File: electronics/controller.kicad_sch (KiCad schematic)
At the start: 81 parts, among them J1 Conn_01x02, J10 Heated_Bed_Thermistor_Connect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, J11 Bl_Touch_Gnd_ZMin_Connector, J12 Bl_Touch_Signal_Vcc_Gnd_Conne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, J13 Motor_A_Connector, J14 Motor_B_Connector, J15 Motor_Z_Connector, J16 Motor_E_Connector, J2 X_Axis_Endstop_Connector, J3 Y_Axis_Endstop_Connector, J4 USB_C_Receptacle_USB2.0, J5 Hotend_Connector, J6 Heated_Bed_Connector, J7 Hotend_Fan_Connector, J8 Layer_Fan_Connector, J9 Hotend_Thermistor_Connector, Q1 PSMN4R1-30YLC, Q2 PSMN4R1-30YLC, Q3 PSMN4R1-30YLC, Q4 PSMN4R1-30YLC, SW1 EN_Button, SW2 Boot_Button, SW3 Pause/Resume_Button, U1 K7803JT-500R3-LB, U2 LMTOE78_05-0.5, U3 ESP32-S3-WROOM-1, U4 MT29F2G01ABAGDWB-IT, U5 USBLC6-2SC6, U6 TMC2209_SILENTSTEPSTICK, U7 TMC2209_SILENTSTEPSTICK, U8 TMC2209_SILENTSTEPSTICK, U9 TMC2209_SILENTSTEPSTICK

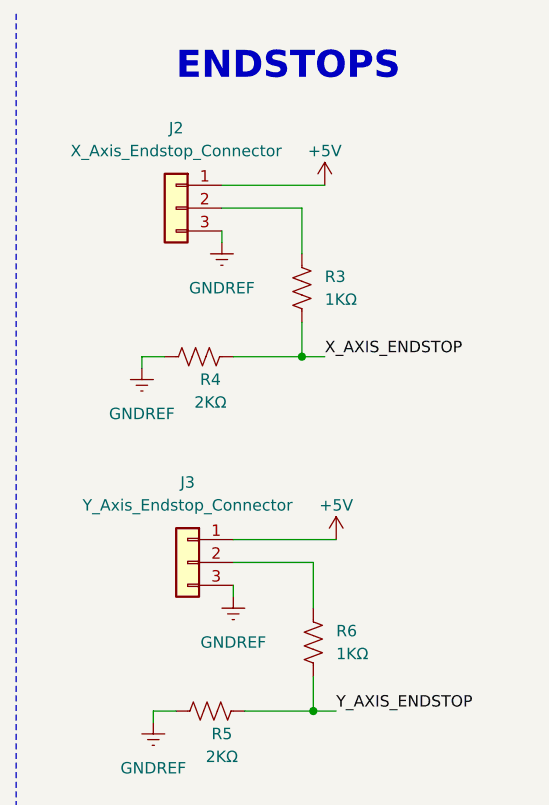
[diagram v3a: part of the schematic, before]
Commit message: ✨ Add filter capacitors to endstops on KiCad schematic
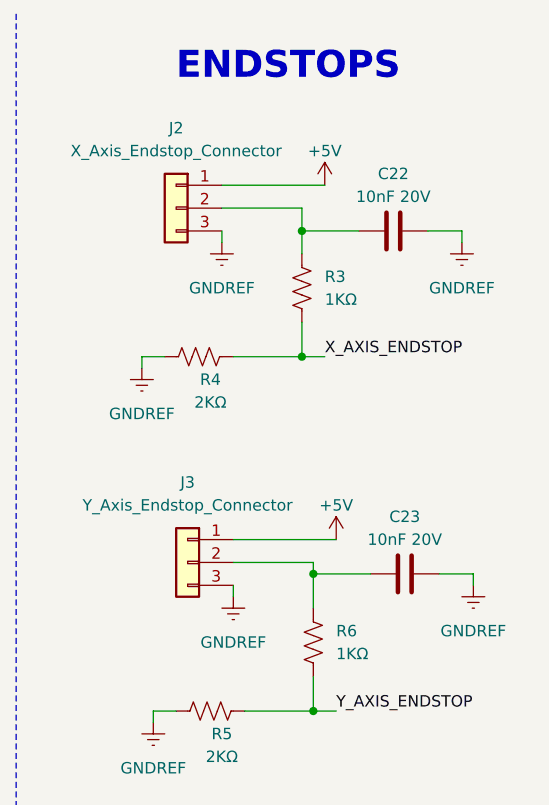
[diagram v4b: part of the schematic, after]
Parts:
- added C22, C23: 10nF 20V, symbol Project:C
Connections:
- net GNDREF: now also C22.2, C23.2
- net at J3.2 (Pin_2), R6.2: now also C23.1
- net at J2.2 (Pin_2), R3.2: now also C22.1
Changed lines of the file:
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@@
   (junction (at 229.87 43.18) (diameter 0) (color 0 0 0 0)
   )
+  (junction (at 383.54 35.56) (diameter 0) (color 0 0 0 0)
+  )
   (junction (at 280.67 229.87) (diameter 0) (color 0 0 0 0)
   )
@@
   (junction (at 121.92 208.28) (diameter 0) (color 0 0 0 0)
   )
+  (junction (at 384.81 73.66) (diameter 0) (color 0 0 0 0)
+  )
   (no_connect (at 256.54 114.3))
   (no_connect (at 43.18 259.08))
@@
     (stroke (width 0) (type default))
   )
-  (wire (pts (xy 384.81 72.39) (xy 384.81 77.47))
+  (wire (pts (xy 384.81 72.39) (xy 384.81 73.66))
     (stroke (width 0) (type default))
   )
@@
     (stroke (width 0) (type default))
   )
+  (wire (pts (xy 389.89 35.56) (xy 383.54 35.56))
+    (stroke (width 0) (type default))
+  )
   (wire (pts (xy 227.33 247.65) (xy 227.33 243.84))
     (stroke (width 0) (type default))
@@
     (stroke (width 0) (type default))
   )
+  (wire (pts (xy 402.59 74.93) (xy 402.59 73.66))
+    (stroke (width 0) (type default))
+  )
   (wire (pts (xy 242.57 247.65) (xy 246.38 247.65))
     (stroke (width 0) (type default))
@@
     (stroke (width 0) (type default))
   )
+  (wire (pts (xy 401.32 36.83) (xy 401.32 35.56))
+    (stroke (width 0) (type default))
+  )
   (wire (pts (xy 80.01 180.34) (xy 86.36 180.34))
     (stroke (width 0) (type default))
@@
     (stroke (width 0) (type dash))
   )
+  (wire (pts (xy 397.51 35.56) (xy 401.32 35.56))
+    (stroke (width 0) (type default))
+  )
   (wire (pts (xy 27.94 248.92) (xy 43.18 248.92))
     (stroke (width 0) (type default))
@@
     (stroke (width 0) (type default))
   )
-  (wire (pts (xy 383.54 33.02) (xy 383.54 38.1))
+  (wire (pts (xy 383.54 33.02) (xy 383.54 35.56))
     (stroke (width 0) (type default))
   )
@@
     (stroke (width 0) (type default))
   )
+  (wire (pts (xy 398.78 73.66) (xy 402.59 73.66))
+    (stroke (width 0) (type default))
+  )
   (wire (pts (xy 44.45 114.3) (xy 64.77 114.3))
     (stroke (width 0) (type default))
@@
     (stroke (width 0) (type default))
   )
+  (wire (pts (xy 384.81 73.66) (xy 384.81 77.47))
+    (stroke (width 0) (type default))
+  )
   (wire (pts (xy 166.37 175.26) (xy 166.37 179.07))
     (stroke (width 0) (type default))
@@
     (stroke (width 0) (type default))
   )
+  (wire (pts (xy 391.16 73.66) (xy 384.81 73.66))
+    (stroke (width 0) (type default))
+  )
   (wire (pts (xy 374.65 187.96) (xy 374.65 190.5))
     (stroke (width 0) (type default))
@@
     (stroke (width 0) (type default))
   )
+  (wire (pts (xy 383.54 35.56) (xy 383.54 38.1))
+    (stroke (width 0) (type default))
+  )
   (wire (pts (xy 113.03 198.12) (xy 124.46 198.12))
     (stroke (width 0) (type default))
@@
     )
   )
+  (symbol (lib_id "Project:GNDREF") (at 402.59 74.93 0) (mirror y) (unit 1)
+    (in_bom yes) (on_board yes) (dnp no)
+    (property "Reference" "#PWR086" (at 402.59 81.28 0)
+      (effects (font (size 1.27 1.27)) hide)
+    )
+    (property "Value" "GNDREF" (at 402.59 80.01 0)
+      (effects (font (size 1.27 1.27)))
+    )
+    (property "Footprint" "" (at 402.59 74.93 0)
+      (effects (font (size 1.27 1.27)) hide)
+    )
+    (property "Datasheet" "" (at 402.59 74.93 0)
+      (effects (font (size 1.27 1.27)) hide)
+    )
+    (pin "1")
+    (instances
+      (project "controller"
+        (path "/b72cfb6e-763f-4aec-88af-02f682ab9e2d"
+          (reference "#PWR086") (unit 1)
+        )
+      )
+    )
+  )
   (symbol (lib_id "Project:USB_C_Receptacle_USB2.0") (at 29.21 114.3 0) (unit 1)
     (in_bom yes) (on_board yes) (dnp no) (fields_autoplaced)
@@
     )
   )
+  (symbol (lib_id "Project:C") (at 393.7 35.56 90) (unit 1)
+    (in_bom yes) (on_board yes) (dnp no)
+    (property "Reference" "C22" (at 393.7 29.21 90)
+      (effects (font (size 1.27 1.27)))
+    )
+    (property "Value" "10nF 20V" (at 393.7 31.75 90)
+      (effects (font (size 1.27 1.27)))
+    )
+    (property "Footprint" "" (at 397.51 34.5948 0)
+      (effects (font (size 1.27 1.27)) hide)
+    )
+    (property "Datasheet" "~" (at 393.7 35.56 0)
+      (effects (font (size 1.27 1.27)) hide)
+    )
+    (pin "1")
+    (pin "2")
+    (instances
+      (project "controller"
+        (path "/b72cfb6e-763f-4aec-88af-02f682ab9e2d"
+          (reference "C22") (unit 1)
+        )
+      )
+    )
+  )
   (symbol (lib_id "Project:Conn_01x04") (at 166.37 251.46 0) (unit 1)
     (in_bom yes) (on_board yes) (dnp no) (fields_autoplaced)
@@
     )
   )
+  (symbol (lib_id "Project:GNDREF") (at 401.32 36.83 0) (mirror y) (unit 1)
+    (in_bom yes) (on_board yes) (dnp no)
+    (property "Reference" "#PWR085" (at 401.32 43.18 0)
+      (effects (font (size 1.27 1.27)) hide)
+    )
+    (property "Value" "GNDREF" (at 401.32 41.91 0)
+      (effects (font (size 1.27 1.27)))
+    )
+    (property "Footprint" "" (at 401.32 36.83 0)
+      (effects (font (size 1.27 1.27)) hide)
+    )
+    (property "Datasheet" "" (at 401.32 36.83 0)
+      (effects (font (size 1.27 1.27)) hide)
+    )
+    (pin "1")
+    (instances
+      (project "controller"
+        (path "/b72cfb6e-763f-4aec-88af-02f682ab9e2d"
+          (reference "#PWR085") (unit 1)
+        )
+      )
+    )
+  )
   (symbol (lib_id "Project:R_US") (at 227.33 264.16 270) (unit 1)
     (in_bom yes) (on_board yes) (dnp no)
@@
         )
       )
+    )
+  )
+  (symbol (lib_id "Project:C") (at 394.97 73.66 90) (unit 1)
+    (in_bom yes) (on_board yes) (dnp no)
+    (property "Reference" "C23" (at 394.97 67.31 90)
+      (effects (font (size 1.27 1.27)))
+    )
+    (property "Value" "10nF 20V" (at 394.97 69.85 90)
+      (effects (font (size 1.27 1.27)))
+    )
+    (property "Footprint" "" (at 398.78 72.6948 0)
+      (effects (font (size 1.27 1.27)) hide)
+    )
+    (property "Datasheet" "~" (at 394.97 73.66 0)
+      (effects (font (size 1.27 1.27)) hide)
+    )
+    (pin "1")
+    (pin "2")
+    (instances
+      (project "controller"
+        (path "/b72cfb6e-763f-4aec-88af-02f682ab9e2d"
+          (reference "C23") (unit 1)
+        )
+      )

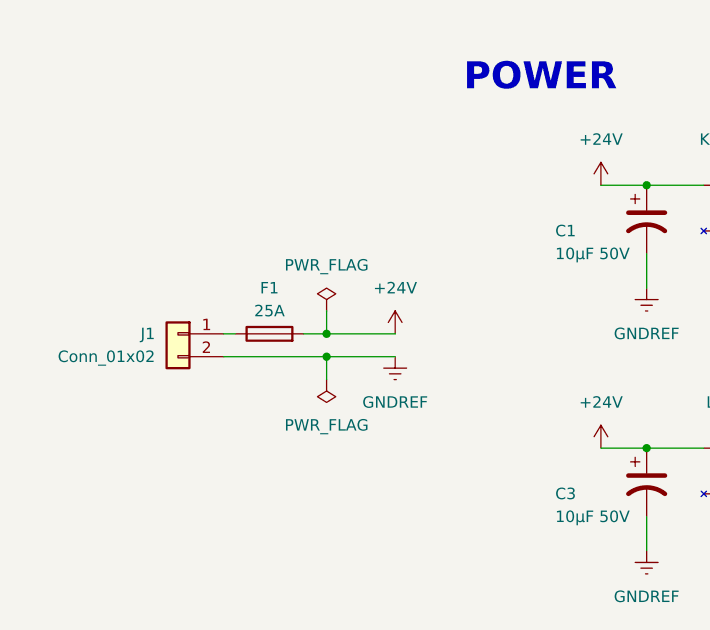
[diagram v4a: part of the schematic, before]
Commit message: ✨ Add reverse voltage protection to power supply connector on KiCad schematic
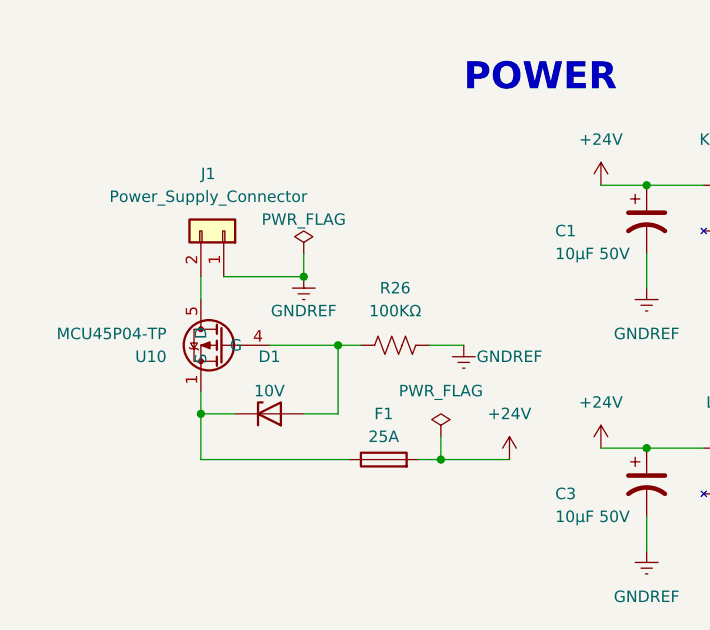
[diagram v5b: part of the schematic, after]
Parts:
- added D1: 10V, symbol Project:D_Zener
- added R26: 100KΩ, symbol Project:R_US
- added U10: MCU45P04-TP, symbol Project:MCU45P04-TP
- J1: value Conn_01x02 -> Power_Supply_Connector
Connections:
- net GNDREF: now also J1.1 (Pin_1), R26.2; no longer J1.2 (Pin_2)
- net at F1.1: now also D1.1 (K), U10.1 (S), U10.2 (S), U10.3 (S); no longer J1.1 (Pin_1)
- new net: D1.2 (A), R26.1, U10.4 (G)
- new net: J1.2 (Pin_2), U10.5 (D)
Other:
- moved on the sheet: F1, J1

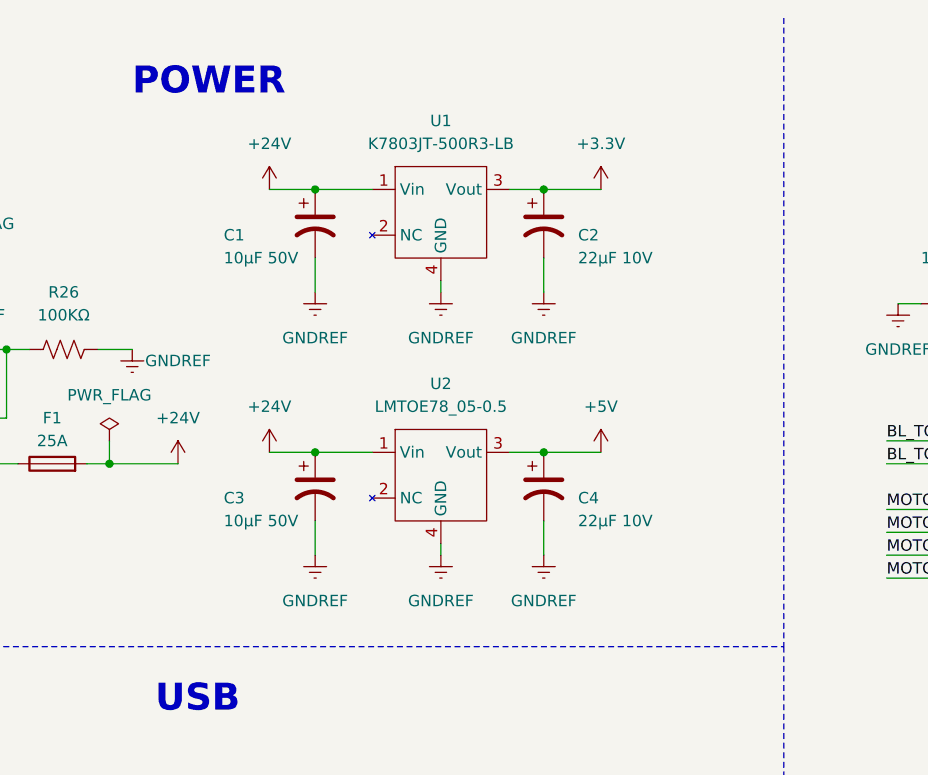
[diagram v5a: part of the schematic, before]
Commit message: ⚡️ Change voltage regulators on KiCad schematic
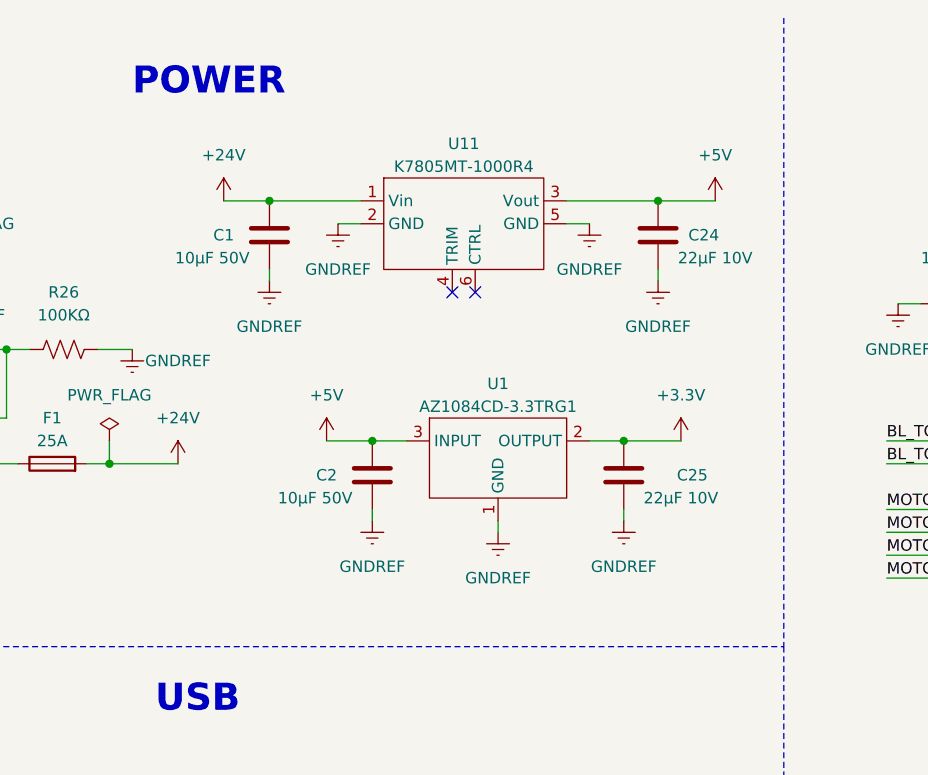
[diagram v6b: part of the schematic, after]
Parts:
- removed C1, C3: 10µF 50V, symbol Project:C_Polarized_US
- removed C2, C4: 22µF 10V, symbol Project:C_Polarized_US
- removed U1: K7803JT-500R3-LB, symbol Project:K7803JT-500R3-LB
- removed U2: LMTOE78_05-0.5, symbol Project:LMTOE78_05-0.5
- added C1, C2: 10µF 50V, symbol Project:C
- added C24, C25: 22µF 10V, symbol Project:C
- added U1: AZ1084CD-3.3TRG1, symbol Project:AZ1084CD-3.3TRG1
- added U11: K7805MT-1000R4, symbol Project:K7805MT-1000R4
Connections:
- net +24V: now also C1.2, U11.1 (Vin)
- net +3.3V: now also C25.2, U1.2 (OUTPUT)
- net +5V: now also C2.2, C24.2, U1.3 (INPUT), U11.3 (Vout)
- net GNDREF: now also C1.1, C2.1, C24.1, C25.1, U1.1 (GND), U11.2 (GND), U11.5 (GND)
- no-connect marks 16 -> 18

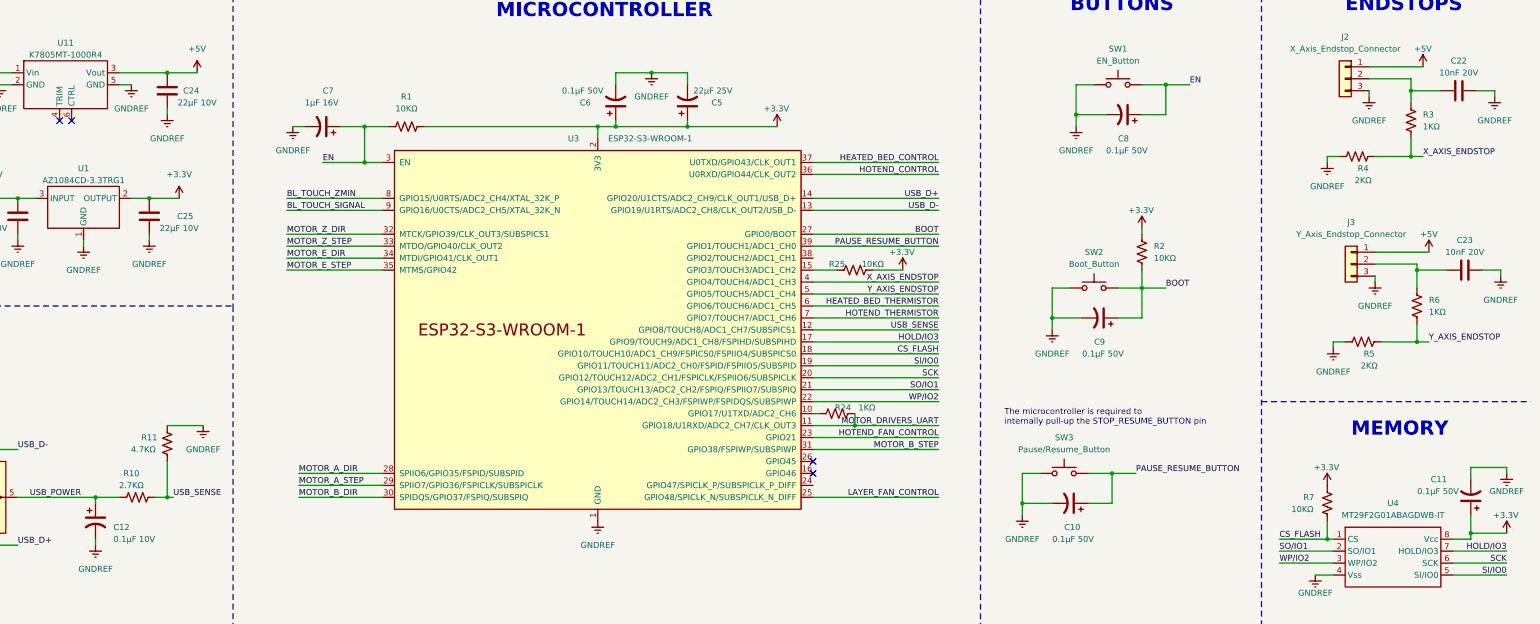
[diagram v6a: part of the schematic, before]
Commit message: ✏️ Replace all the capacitors' symbols with the appropriate ones on KiCad schematic
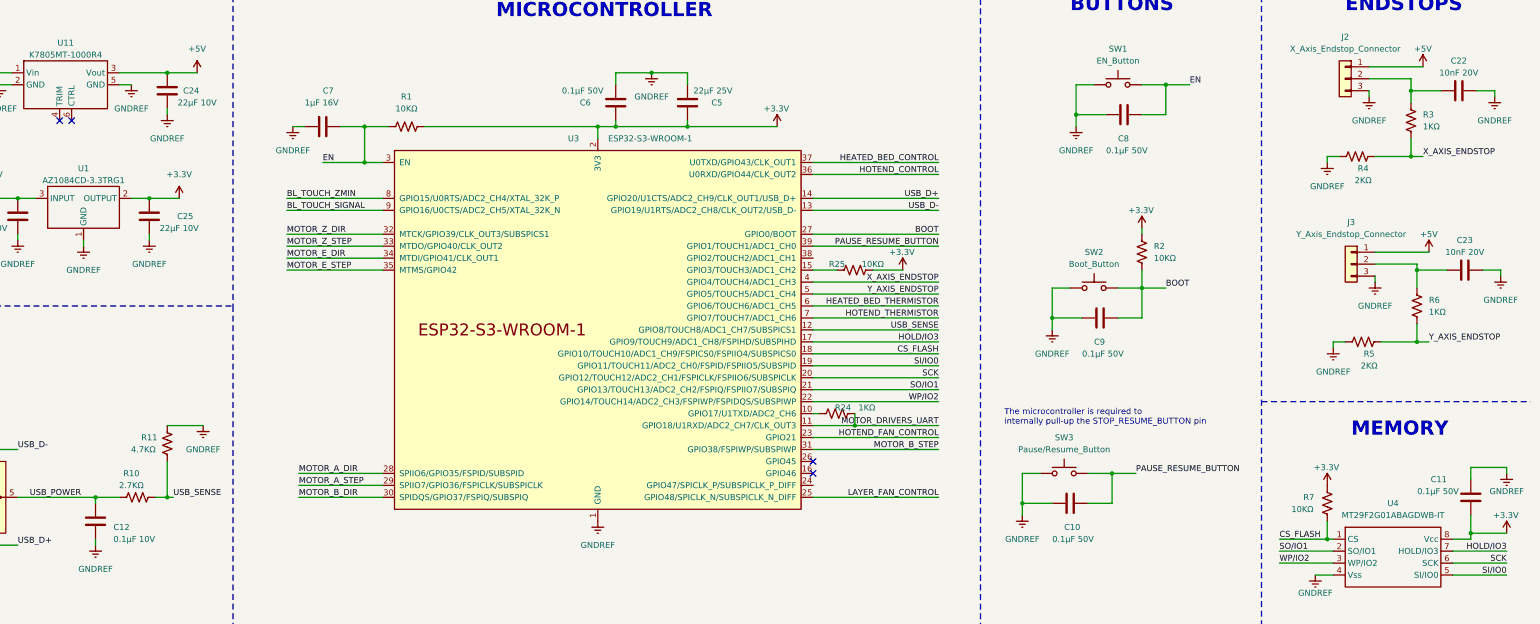
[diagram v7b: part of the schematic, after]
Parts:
- C10, C11, C12, C5, C6, C7, C8, C9: symbol Project:C_Polarized_US -> Project:C
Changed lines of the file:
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@@
     )
   )
-  (symbol (lib_id "Project:C_Polarized_US") (at 214.63 38.1 0) (mirror x) (unit 1)
+  (symbol (lib_id "Project:C") (at 214.63 38.1 0) (mirror x) (unit 1)
     (in_bom yes) (on_board yes) (dnp no)
     (property "Reference" "C6" (at 207.01 38.1 0)
@@
       (effects (font (size 1.27 1.27)) (justify left))
     )
-    (property "Footprint" "" (at 214.63 38.1 0)
+    (property "Footprint" "" (at 215.5952 34.29 0)
       (effects (font (size 1.27 1.27)) hide)
     )
@@
     )
   )
-  (symbol (lib_id "Project:C_Polarized_US") (at 152.4 43.18 270) (mirror x) (unit 1)
+  (symbol (lib_id "Project:C") (at 152.4 43.18 270) (mirror x) (unit 1)
     (in_bom yes) (on_board yes) (dnp no)
     (property "Reference" "C7" (at 152.4 35.56 90)
@@
       (effects (font (size 1.27 1.27)) (justify left))
     )
-    (property "Footprint" "" (at 152.4 43.18 0)
+    (property "Footprint" "" (at 148.59 42.2148 0)
       (effects (font (size 1.27 1.27)) hide)
     )
@@
     )
   )
-  (symbol (lib_id "Project:C_Polarized_US") (at 322.58 40.64 270) (mirror x) (unit 1)
+  (symbol (lib_id "Project:C") (at 322.58 40.64 270) (mirror x) (unit 1)
     (in_bom yes) (on_board yes) (dnp no)
     (property "Reference" "C8" (at 321.31 45.72 90)
@@
       (effects (font (size 1.27 1.27)) (justify left))
     )
-    (property "Footprint" "" (at 322.58 40.64 0)
+    (property "Footprint" "" (at 318.77 39.6748 0)
       (effects (font (size 1.27 1.27)) hide)
     )
@@
     )
   )
-  (symbol (lib_id "Project:C_Polarized_US") (at 104.14 127 0) (unit 1)
+  (symbol (lib_id "Project:C") (at 104.14 127 0) (unit 1)
     (in_bom yes) (on_board yes) (dnp no)
     (property "Reference" "C12" (at 107.95 128.27 0)
@@
       (effects (font (size 1.27 1.27)) (justify left))
     )
-    (property "Footprint" "" (at 104.14 127 0)
+    (property "Footprint" "" (at 105.1052 130.81 0)
       (effects (font (size 1.27 1.27)) hide)
     )
@@
     )
   )
-  (symbol (lib_id "Project:C_Polarized_US") (at 311.15 123.19 270) (mirror x) (unit 1)
+  (symbol (lib_id "Project:C") (at 311.15 123.19 270) (mirror x) (unit 1)
     (in_bom yes) (on_board yes) (dnp no)
     (property "Reference" "C10" (at 309.88 128.27 90)
@@
       (effects (font (size 1.27 1.27)) (justify left))
     )
-    (property "Footprint" "" (at 311.15 123.19 0)
+    (property "Footprint" "" (at 307.34 122.2248 0)
       (effects (font (size 1.27 1.27)) hide)
     )
@@
     )
   )
-  (symbol (lib_id "Project:C_Polarized_US") (at 229.87 38.1 0) (mirror x) (unit 1)
+  (symbol (lib_id "Project:C") (at 229.87 38.1 0) (mirror x) (unit 1)
     (in_bom yes) (on_board yes) (dnp no)
     (property "Reference" "C5" (at 234.95 38.1 0)
@@
       (effects (font (size 1.27 1.27)) (justify left))
     )
-    (property "Footprint" "" (at 229.87 38.1 0)
+    (property "Footprint" "" (at 230.8352 34.29 0)
       (effects (font (size 1.27 1.27)) hide)
     )
@@
     )
   )
-  (symbol (lib_id "Project:C_Polarized_US") (at 317.5 83.82 270) (mirror x) (unit 1)
+  (symbol (lib_id "Project:C") (at 317.5 83.82 270) (mirror x) (unit 1)
     (in_bom yes) (on_board yes) (dnp no)
     (property "Reference" "C9" (at 316.23 88.9 90)
@@
       (effects (font (size 1.27 1.27)) (justify left))
     )
-    (property "Footprint" "" (at 317.5 83.82 0)
+    (property "Footprint" "" (at 313.69 82.8548 0)
       (effects (font (size 1.27 1.27)) hide)
     )
@@
     )
   )
-  (symbol (lib_id "Project:C_Polarized_US") (at 396.24 121.92 180) (unit 1)
+  (symbol (lib_id "Project:C") (at 396.24 121.92 180) (unit 1)
     (in_bom yes) (on_board yes) (dnp no)
     (property "Reference" "C11" (at 391.16 118.11 0)
@@
       (effects (font (size 1.27 1.27)) (justify left))
     )
-    (property "Footprint" "" (at 396.24 121.92 0)
+    (property "Footprint" "" (at 395.2748 118.11 0)
       (effects (font (size 1.27 1.27)) hide)
     )
